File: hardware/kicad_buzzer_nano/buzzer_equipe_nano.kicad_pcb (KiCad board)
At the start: 2 copper layers, 120 x 140 mm, 9 parts, among them J1 nRF24L01+PA+LNA - VERIFIER le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, J2 Module charge TP4056+protect+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, J3 Module vibreur IN/VCC/GND, SW1 Bouton BUZZ (fils volants), SW2 Interrupteur marche/arret (fi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

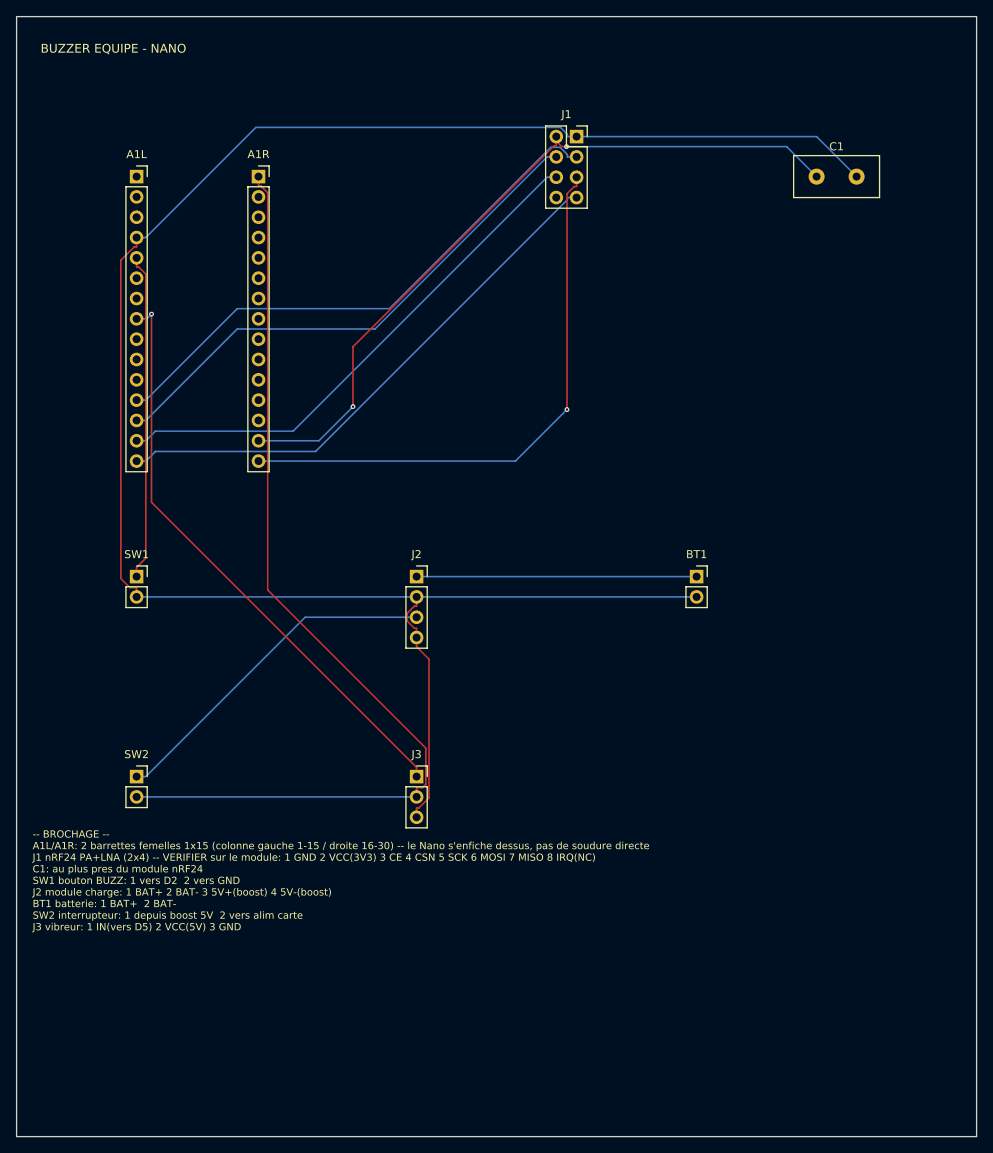
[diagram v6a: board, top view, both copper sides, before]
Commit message: hardware: cartes retrecies, guide serigraphie retire, keepout sous le nRF24
3 demandes traitees sur les 3 cartes:

- Retrait du texte-guide en serigraphie (bloc BROCHAGE) -- n'a plus sa
  place sur un circuit destine a la fabrication reelle. Repere de
  composant standard (A1L, J1, C1...) conserve, paragraphe d'instructions
  retire.
- Cartes nettement plus compactes: nano 125x145 -> 90x100mm, hub
  185x145 -> 137x85mm, esp32 130x145 -> 68x101mm.
- Nano/hub: C1/C3 (decouplage nRF24) rapproches encore plus de J1/J_NRF.
- Zone sans cuivre (keepout, pistes/vias/plans interdits sur F.Cu ET B.Cu)
  ajoutee sous l'emplacement du module nRF24 PA+LNA sur les 2 cartes qui en
  ont un (nano, hub) -- pas de cuivre sous l'antenne du module. Verifie
  reellement respecte par Freerouting (pas juste accepte par kicad-cli):
  un test dedie avec un keepout bloquant deliberement le seul chemin entre
  2 pastilles a fait router 0 piste par l'autorouteur, preuve qu'il n'etait
  pas ignore. Premiere disposition (keepout collant a J1 sur plusieurs
  cotes) a bloque le routeur (8 pistes indefiniment non routees apres 100+
  passes) -- corrige en placant le keepout en presqu'ile contre le bord de
  la carte, ne bloquant aucun chemin de routage necessaire.

Les 3 cartes re-routees (Freerouting) et revalidees (kicad-cli pcb drc):
0 violation de clearance, 0 element non connecte, 0 track_dangling sur les
3, et 0 piste a l'interieur des zones keepout (verifie par script).

Co-Authored-By: Claude Sonnet 5 <noreply@anthropic.com>
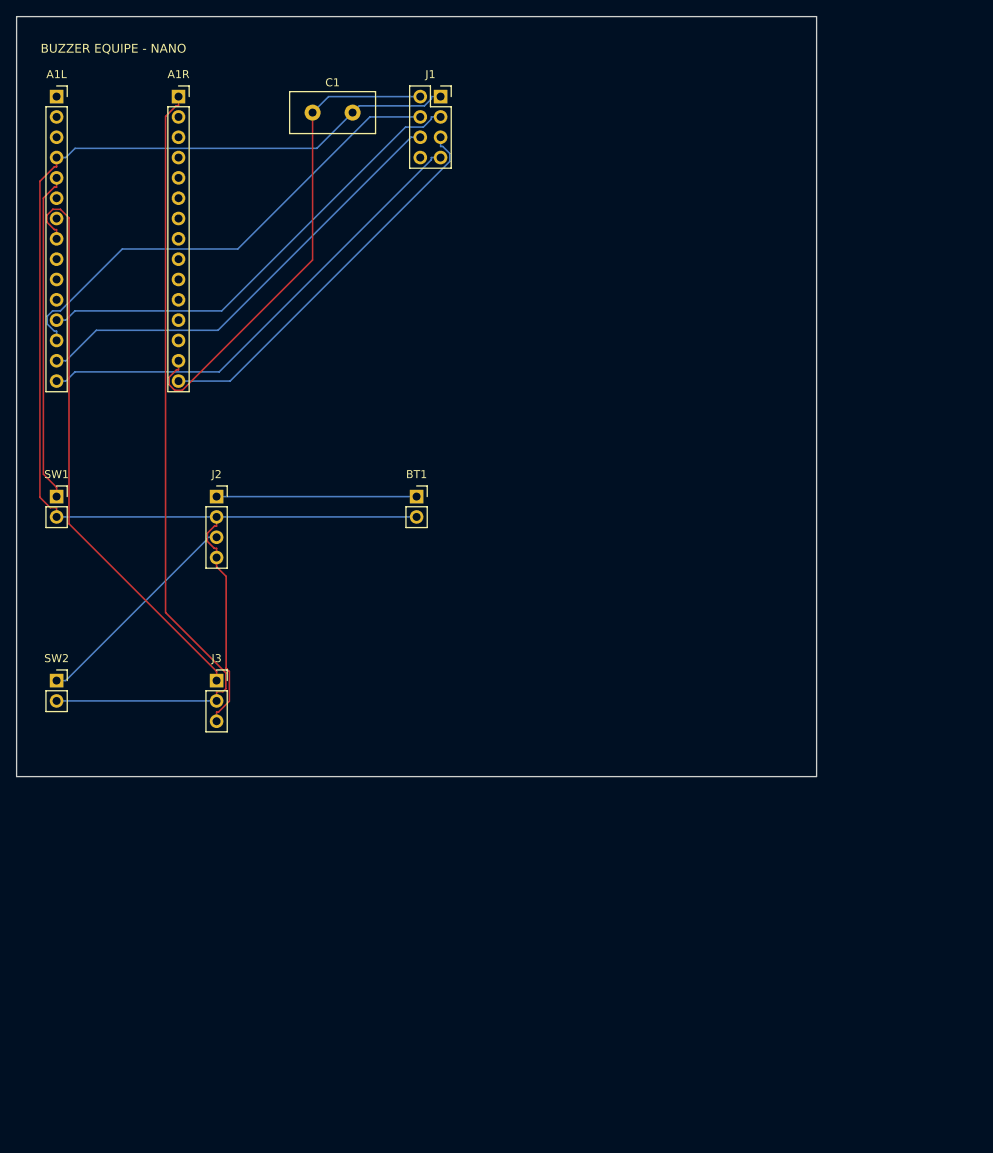
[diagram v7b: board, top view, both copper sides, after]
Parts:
- C1: value 10-100uF decouplage nRF24 (obligatoire) -> 10-100uF decouplage nRF24 (obligatoire, au plus pres)
- moved C1 63.5 mm to (42.0, 17.0)
- moved BT1 36.4 mm to (55.0, 65.0)
- moved J3 27.7 mm to (30.0, 88.0)
- moved J2 26.9 mm to (30.0, 65.0)
- moved J1 17.7 mm to (58.0, 15.0)
- moved SW2 15.6 mm to (10.0, 88.0)
- moved A1R 14.1 mm to (25.2, 15.0)
- moved A1L 14.1 mm to (10.0, 15.0)
- moved SW1 14.1 mm to (10.0, 65.0)
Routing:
- net GND: track 245.9 -> 172.1 mm
- net +3V3: track 92.5 -> 61.3 mm, vias 2 -> 0
- net NRF_SCK: track 70.9 -> 49.0 mm, vias 1 -> 0
- net VCC_5V_SW: track 122.3 -> 100.4 mm
- net VCC_5V_RAW: track 43.3 -> 27.6 mm
- net NRF_CE: track 68.8 -> 58.7 mm
- net BAT_PLUS: track 35.0 -> 25.0 mm
- net NRF_MOSI: track 66.1 -> 57.0 mm
- net NRF_MISO: track 68.8 -> 59.7 mm
- net NRF_CSN: track 66.1 -> 60.6 mm
- net VIBE_IN: track 73.7 -> 72.6 mm, vias 1 -> 0
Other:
- board size 120 x 140 mm -> 100 x 95 mm
- board text removed: "-- BROCHAGE -- A1L/A1R: 2 barrettes femelles 1x15 (colonne gauche 1-15 / droite 16-30) -- le Nano s'enfiche dessus, pas de soudure directe J1 nRF24 PA+LNA (2x4) -- VERIFIER sur le module: 1 GND 2 VCC(3V3) 3 CE 4 CSN 5 SCK 6 MOSI 7 MISO 8 IRQ(NC) C1: au plus pres du module nRF24 SW1 bouton BUZZ: 1 vers D2 2 vers GND J2 module charge: 1 BAT+ 2 BAT- 3 5V+(boost) 4 5V-(boost) BT1 batterie: 1 BAT+ 2 B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"

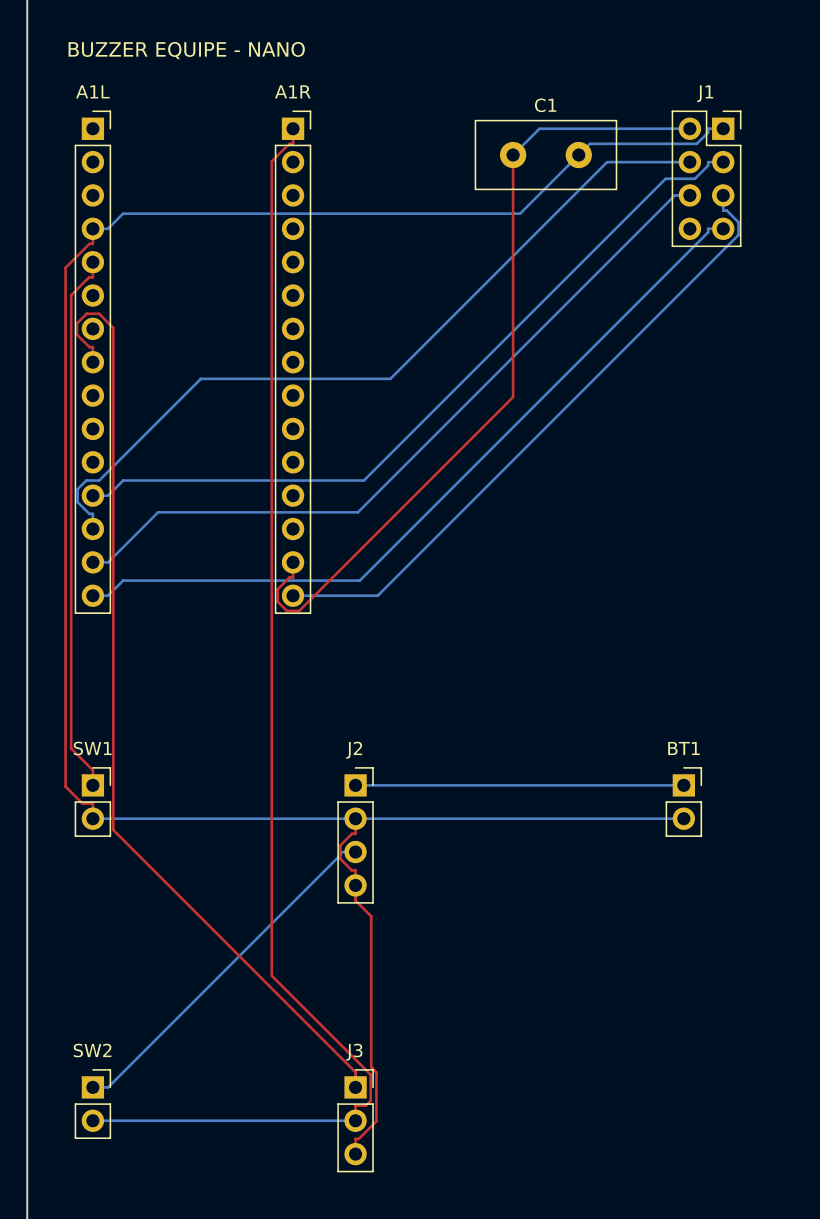
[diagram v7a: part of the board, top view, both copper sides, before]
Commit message: hardware: J1/J_NRF en broches males (le module nRF24 a des ports femelles)
Le module nRF24L01+PA+LNA a lui-meme des ports femelles sur son connecteur
2x4 -- l'empreinte utilisee jusqu'ici (PinSocket_2x04, femelle cote carte)
etait donc a l'envers. Change en PinHeader_2x04 (broches MALES) sur les 2
cartes concernees (nano, hub), pour que le module s'enfiche directement
dessus -- logique inverse de A1L/A1R (Nano) et U_ESP32L/R ou U1L/U1R (ESP32)
dont les modules ont eux-memes des broches males.

Le footprint male a son empreinte MIROIR par rapport au femelle (pastille 2
a +2.54mm au lieu de -2.54mm) -- numerotation de broche inchangee (1=GND,
2=VCC... comme deja verifie), seule la position physique change. Ajuste de
quelques mm la position de J1/J_NRF et de la zone keepout pour garder le
meme espacement de securite avec le nouveau contour de composant.

Les 2 cartes re-routees (Freerouting) et revalidees (kicad-cli pcb drc):
0 violation de clearance, 0 element non connecte, 0 piste dans la zone
keepout (verifie par script), 0 track_dangling apres nettoyage des residus
d'autorouter habituels sur la carte hub.

Co-Authored-By: Claude Sonnet 5 <noreply@anthropic.com>
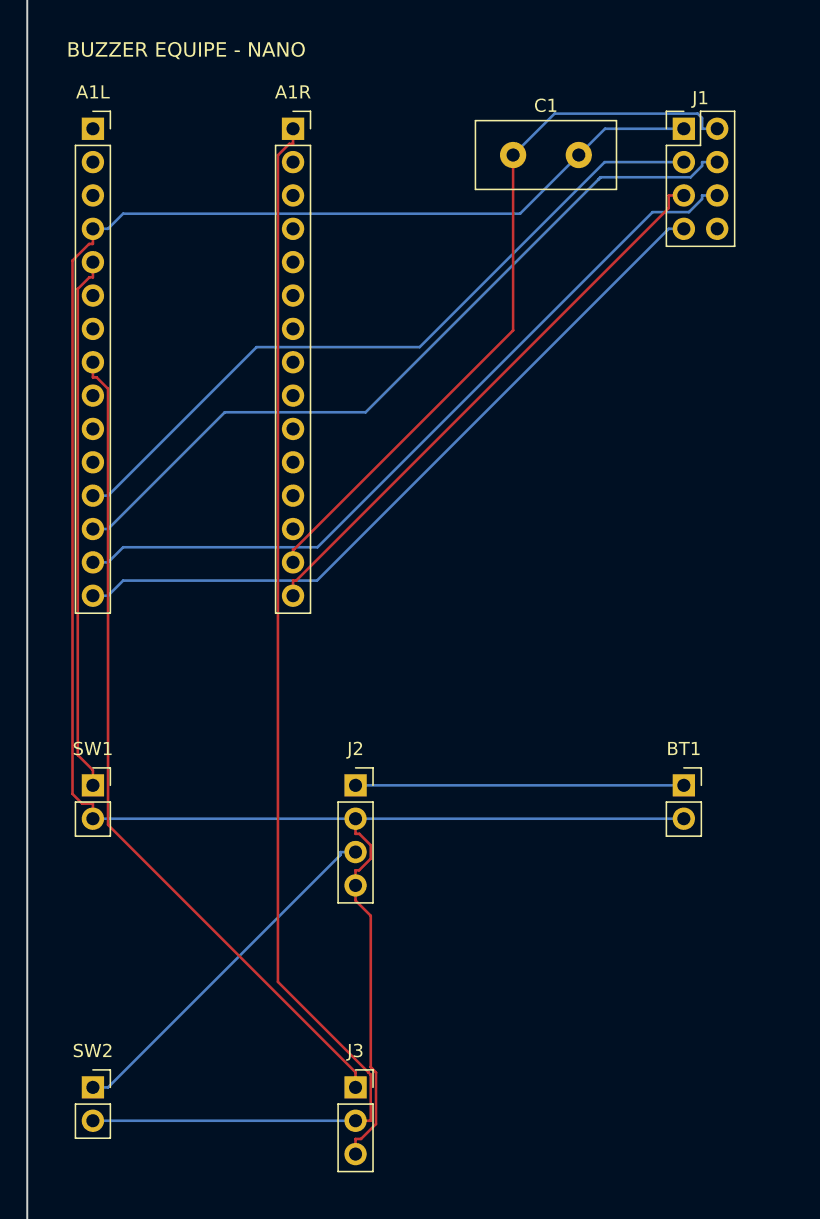
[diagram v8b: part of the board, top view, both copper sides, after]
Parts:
- J1: value nRF24L01+PA+LNA - VERIFIER le brochage sur le module recu -> nRF24L01+PA+LNA (broches MALES, le module a des ports femelles) - VERIFIER le brochage sur le module recu; footprint Connector_PinSocket_2.54mm:PinSocket_2x04_P2.54mm_Vertical -> Connector_PinHeader_2.54mm:PinHeader_2x04_P2.54mm_Vertical
- moved J1 3.00 mm to (55.0, 15.0)
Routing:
- net VIBE_IN: track 72.6 -> 63.7 mm
- net +3V3: track 61.3 -> 55.8 mm
- net NRF_SCK: track 49.0 -> 43.6 mm
- net GND: track 172.1 -> 168.6 mm
- net NRF_MISO: track 59.7 -> 56.6 mm
- net NRF_CE: track 58.7 -> 55.5 mm
- net NRF_MOSI: track 57.0 -> 59.3 mm
- net NRF_CSN: track 60.6 -> 59.5 mm
